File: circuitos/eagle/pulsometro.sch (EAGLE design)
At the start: 35 parts, among them IC1 LM358N, IC2 LM358N, IC3 PIC18F2550_28DIP, T1 BC547, X1 20MHz

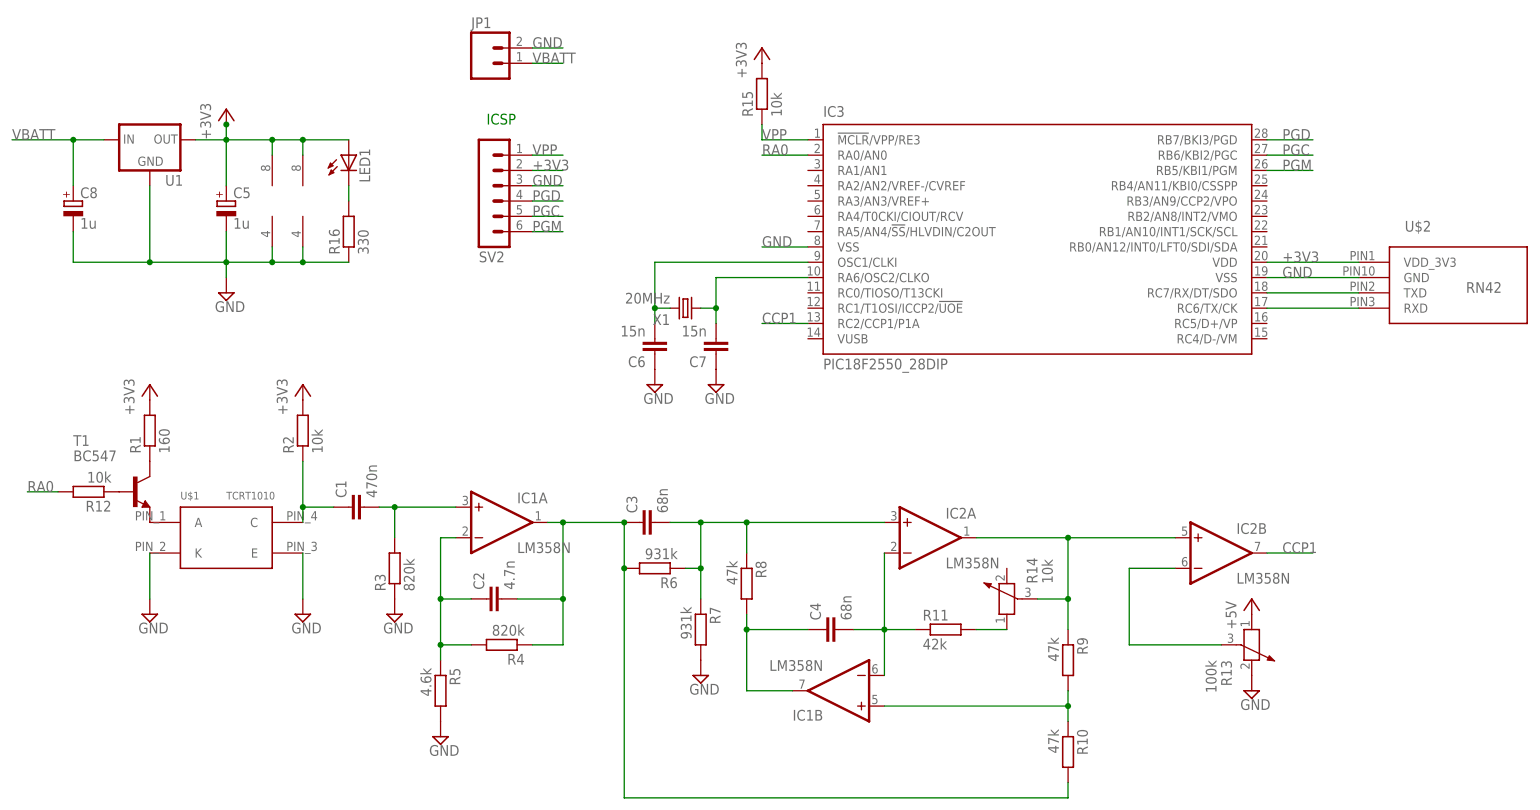
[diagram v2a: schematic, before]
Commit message: Update circuit
* Remove transistor switch of TCRT1010 diode and change resistor value
* Change LM358 op-amp to TLV2472
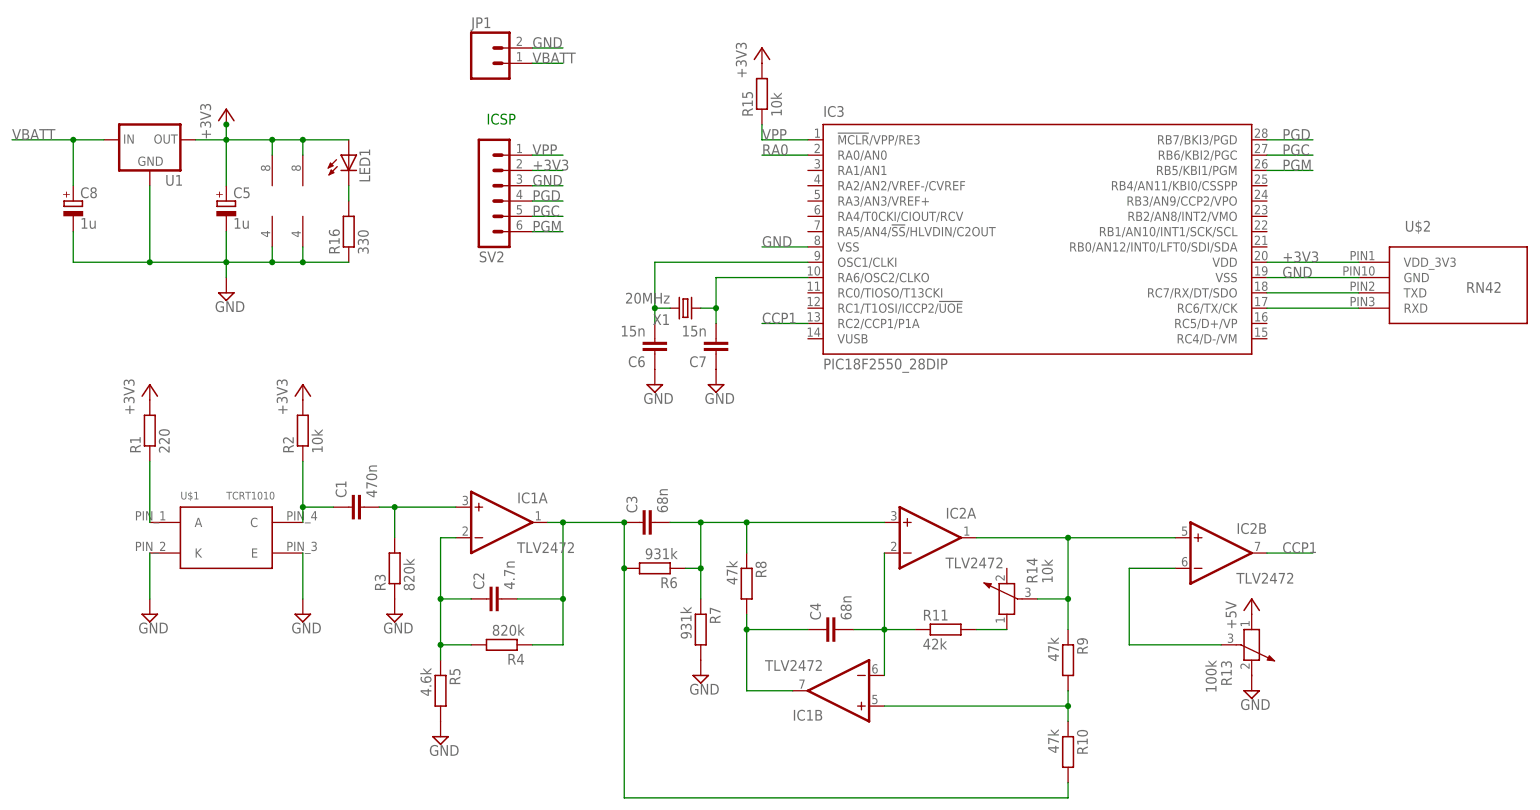
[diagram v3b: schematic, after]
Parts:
- removed R12: 10k, rcl:R-EU_0204/7
- removed T1: BC547, transistor:BC547
- IC1, IC2: value LM358N -> TLV2472
- R1: value 160 -> 220
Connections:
- removed net N$2: T1.E, U$1.A
- removed net N$7: R12.1, T1.B
- net N$1: now also U$1.A; no longer T1.C
- net RA0: no longer R12.2
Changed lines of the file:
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@@
 <grid distance="0.1" unitdist="inch" unit="inch" style="lines" multiple="1" display="no" altdistance="0.01" altunitdist="inch" altunit="inch"/>
 <layers>
-<layer number="1" name="Top" color="4" fill="1" visible="no" active="no"/>
-<layer number="16" name="Bottom" color="1" fill="1" visible="no" active="no"/>
-<layer number="17" name="Pads" color="2" fill="1" visible="no" active="no"/>
-<layer number="18" name="Vias" color="2" fill="1" visible="no" active="no"/>
-<layer number="19" name="Unrouted" color="6" fill="1" visible="no" active="no"/>
-<layer number="20" name="Dimension" color="15" fill="1" visible="no" active="no"/>
-<layer number="21" name="tPlace" color="16" fill="1" visible="no" active="no"/>
-<layer number="22" name="bPlace" color="14" fill="1" visible="no" active="no"/>
-<layer number="23" name="tOrigins" color="15" fill="1" visible="no" active="no"/>
-<layer number="24" name="bOrigins" color="15" fill="1" visible="no" active="no"/>
-<layer number="25" name="tNames" color="7" fill="1" visible="no" active="no"/>
-<layer number="26" name="bNames" color="7" fill="1" visible="no" active="no"/>
-<layer number="27" name="tValues" color="7" fill="1" visible="no" active="no"/>
-<layer number="28" name="bValues" color="7" fill="1" visible="no" active="no"/>
+<layer number="1" name="Top" color="4" fill="1" visible="yes" active="no"/>
+<layer number="16" name="Bottom" color="1" fill="1" visible="yes" active="no"/>
+<layer number="17" name="Pads" color="2" fill="1" visible="yes" active="no"/>
+<layer number="18" name="Vias" color="2" fill="1" visible="yes" active="no"/>
+<layer number="19" name="Unrouted" color="6" fill="1" visible="yes" active="no"/>
+<layer number="20" name="Dimension" color="15" fill="1" visible="yes" active="no"/>
+<layer number="21" name="tPlace" color="16" fill="1" visible="yes" active="no"/>
+<layer number="22" name="bPlace" color="14" fill="1" visible="yes" active="no"/>
+<layer number="23" name="tOrigins" color="15" fill="1" visible="yes" active="no"/>
+<layer number="24" name="bOrigins" color="15" fill="1" visible="yes" active="no"/>
+<layer number="25" name="tNames" color="7" fill="1" visible="yes" active="no"/>
+<layer number="26" name="bNames" color="7" fill="1" visible="yes" active="no"/>
+<layer number="27" name="tValues" color="7" fill="1" visible="yes" active="no"/>
+<layer number="28" name="bValues" color="7" fill="1" visible="yes" active="no"/>
 <layer number="29" name="tStop" color="7" fill="3" visible="no" active="no"/>
 <layer number="30" name="bStop" color="7" fill="6" visible="no" active="no"/>
@@
 <layer number="35" name="tGlue" color="7" fill="4" visible="no" active="no"/>
 <layer number="36" name="bGlue" color="7" fill="5" visible="no" active="no"/>
-<layer number="37" name="tTest" color="7" fill="1" visible="no" active="no"/>
-<layer number="38" name="bTest" color="7" fill="1" visible="no" active="no"/>
+<layer number="37" name="tTest" color="7" fill="1" visible="yes" active="no"/>
+<layer number="38" name="bTest" color="7" fill="1" visible="yes" active="no"/>
 <layer number="39" name="tKeepout" color="4" fill="11" visible="no" active="no"/>
 <layer number="40" name="bKeepout" color="1" fill="11" visible="no" active="no"/>
@@
 <layer number="44" name="Drills" color="7" fill="1" visible="no" active="no"/>
 <layer number="45" name="Holes" color="7" fill="1" visible="no" active="no"/>
-<layer number="46" name="Milling" color="3" fill="1" visible="no" active="no"/>
-<layer number="47" name="Measures" color="7" fill="1" visible="no" active="no"/>
-<layer number="48" name="Document" color="7" fill="1" visible="no" active="no"/>
-<layer number="49" name="Reference" color="7" fill="1" visible="no" active="no"/>
-<layer number="50" name="dxf" color="7" fill="1" visible="no" active="no"/>
-<layer number="51" name="tDocu" color="6" fill="1" visible="no" active="no"/>
-<layer number="52" name="bDocu" color="7" fill="1" visible="no" active="no"/>
-<layer number="53" name="tGND_GNDA" color="7" fill="9" visible="no" active="no"/>
-<layer number="54" name="bGND_GNDA" color="1" fill="9" visible="no" active="no"/>
-<layer number="56" name="wert" color="7" fill="1" visible="no" active="no"/>
-<layer number="57" name="tCAD" color="7" fill="1" visible="no" active="no"/>
-<layer number="59" name="tCarbon" color="7" fill="1" visible="no" active="no"/>
-<layer number="60" name="bCarbon" color="7" fill="1" visible="no" active="no"/>
+<layer number="46" name="Milling" color="3" fill="1" visible="yes" active="no"/>
+<layer number="47" name="Measures" color="7" fill="1" visible="yes" active="no"/>
+<layer number="48" name="Document" color="7" fill="1" visible="yes" active="no"/>
+<layer number="49" name="Reference" color="7" fill="1" visible="yes" active="no"/>
+<layer number="50" name="dxf" color="7" fill="1" visible="yes" active="no"/>
+<layer number="51" name="tDocu" color="6" fill="1" visible="yes" active="no"/>
+<layer number="52" name="bDocu" color="7" fill="1" visible="yes" active="no"/>
+<layer number="53" name="tGND_GNDA" color="7" fill="9" visible="yes" active="no"/>
+<layer number="54" name="bGND_GNDA" color="1" fill="9" visible="yes" active="no"/>
+<layer number="56" name="wert" color="7" fill="1" visible="yes" active="no"/>
+<layer number="57" name="tCAD" color="7" fill="1" visible="yes" active="no"/>
+<layer number="59" name="tCarbon" color="7" fill="1" visible="yes" active="no"/>
+<layer number="60" name="bCarbon" color="7" fill="1" visible="yes" active="no"/>
 <layer number="90" name="Modules" color="5" fill="1" visible="yes" active="yes"/>
 <layer number="91" name="Nets" color="2" fill="1" visible="yes" active="yes"/>
@@
 <part name="SUPPLY4" library="supply2" deviceset="GND" device=""/>
 <part name="P+1" library="supply1" deviceset="+3V3" device=""/>
-<part name="R1" library="rcl" deviceset="R-EU_" device="0204/7" value="160"/>
+<part name="R1" library="rcl" deviceset="R-EU_" device="0204/7" value="220"/>
 <part name="R2" library="rcl" deviceset="R-EU_" device="0204/7" value="10k"/>
-<part name="T1" library="transistor" deviceset="BC547" device=""/>
 <part name="C1" library="rcl" deviceset="C-EU" device="025-025X050" value="470n"/>
 <part name="C2" library="rcl" deviceset="C-EU" device="025-025X050" value="4.7n"/>
@@
 <part name="SUPPLY1" library="supply2" deviceset="GND" device=""/>
 <part name="SUPPLY2" library="supply2" deviceset="GND" device=""/>
-<part name="IC1" library="linear" deviceset="LM358" device="N"/>
+<part name="IC1" library="linear" deviceset="LM358" device="N" value="TLV2472"/>
 <part name="SUPPLY5" library="supply2" deviceset="GND" device=""/>
 <part name="R6" library="rcl" deviceset="R-EU_" device="0204/7" value="931k"/>
@@
 <part name="R10" library="rcl" deviceset="R-EU_" device="0204/7" value="47k"/>
 <part name="R11" library="rcl" deviceset="R-EU_" device="0204/7" value="42k"/>
-<part name="R12" library="rcl" deviceset="R-EU_" device="0204/7" value="10k"/>
 <part name="C3" library="rcl" deviceset="C-EU" device="025-025X050" value="68n"/>
 <part name="C4" library="rcl" deviceset="C-EU" device="025-025X050" value="68n"/>
-<part name="IC2" library="linear" deviceset="LM358" device="N"/>
+<part name="IC2" library="linear" deviceset="LM358" device="N" value="TLV2472"/>
 <part name="R13" library="rcl" deviceset="POTENTIOMETER_" device="PT-10" value="100k"/>
 <part name="R14" library="rcl" deviceset="POTENTIOMETER_" device="PT-10" value="10k"/>
@@
 <instance part="R1" gate="G$1" x="20.32" y="38.1" rot="R90"/>
 <instance part="R2" gate="G$1" x="45.72" y="38.1" rot="R90"/>
-<instance part="T1" gate="G$1" x="17.78" y="27.94"/>
 <instance part="C1" gate="G$1" x="53.34" y="25.4" rot="R90"/>
 <instance part="C2" gate="G$1" x="76.2" y="10.16" rot="R90"/>
@@
 <instance part="R10" gate="G$1" x="172.72" y="-15.24" rot="R270"/>
 <instance part="R11" gate="G$1" x="152.4" y="5.08"/>
-<instance part="R12" gate="G$1" x="10.16" y="27.94" rot="R180"/>
 <instance part="C3" gate="G$1" x="101.6" y="22.86" rot="R90"/>
 <instance part="C4" gate="G$1" x="132.08" y="5.08" rot="R90"/>
@@
 </busses>
 <nets>
-<net name="N$1" class="0">
-<segment>
-<pinref part="R1" gate="G$1" pin="1"/>
-<pinref part="T1" gate="G$1" pin="C"/>
-</segment>
-</net>
-<net name="N$2" class="0">
-<segment>
-<pinref part="U$1" gate="G$1" pin="A"/>
-<pinref part="T1" gate="G$1" pin="E"/>
-</segment>
-</net>
 <net name="+3V3" class="0">
 <segment>
@@
 </segment>
 </net>
-<net name="N$7" class="0">
-<segment>
-<pinref part="T1" gate="G$1" pin="B"/>
-<pinref part="R12" gate="G$1" pin="1"/>
-</segment>
-</net>
 <net name="RA0" class="0">
-<segment>
-<pinref part="R12" gate="G$1" pin="2"/>
-<wire x1="5.08" y1="27.94" x2="0" y2="27.94" width="0.1524" layer="91"/>
-<label x="0" y="27.94" size="1.778" layer="95"/>
-</segment>
 <segment>
 <pinref part="IC3" gate="G$1" pin="RA0/AN0"/>
@@
 </segment>
 </net>
+<net name="N$1" class="0">
+<segment>
+<pinref part="U$1" gate="G$1" pin="A"/>
+<pinref part="R1" gate="G$1" pin="1"/>
+<wire x1="20.32" y1="22.86" x2="20.32" y2="33.02" width="0.1524" layer="91"/>
+</segment>
+</net>

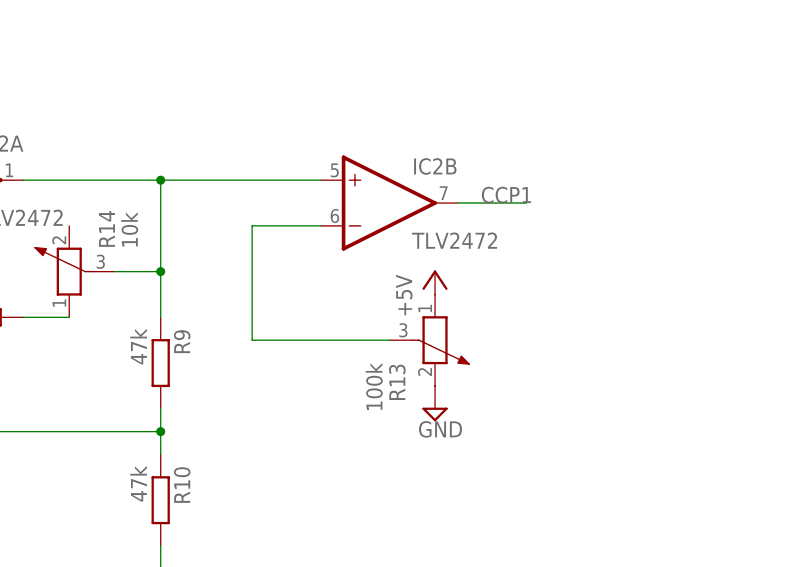
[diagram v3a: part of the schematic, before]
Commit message: Fix voltage source value
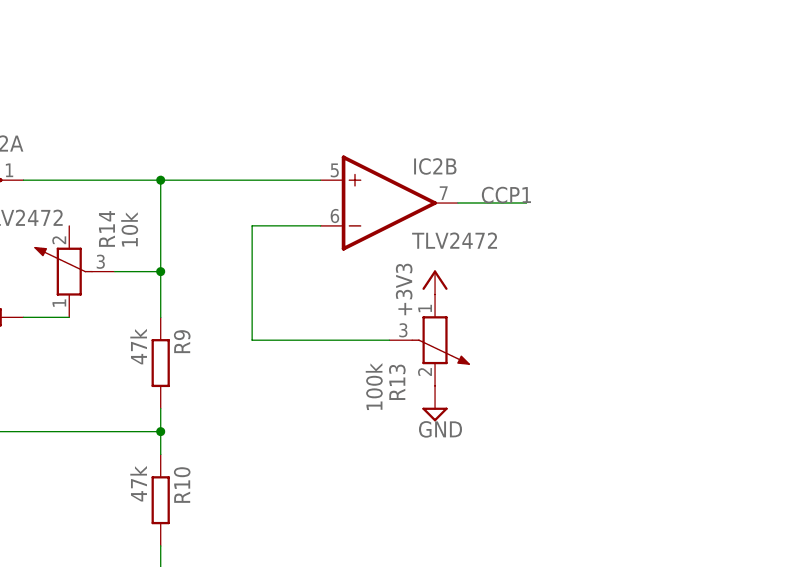
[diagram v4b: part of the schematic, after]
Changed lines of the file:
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@@
 <part name="R14" library="rcl" deviceset="POTENTIOMETER_" device="PT-10" value="10k"/>
 <part name="SUPPLY7" library="supply2" deviceset="GND" device=""/>
-<part name="P+5" library="supply1" deviceset="+5V" device=""/>
 <part name="SUPPLY8" library="supply2" deviceset="GND" device=""/>
 <part name="IC3" library="microchip" deviceset="PIC18F2*_28" device="DIP" technology="550"/>
@@
 <part name="U1" library="SparkFun-PowerIC" deviceset="V_REG_78XX" device="TO-92_UNTESTED"/>
 <part name="C8" library="rcl" deviceset="CPOL-EU" device="E2.5-5" value="1u"/>
+<part name="P+5" library="supply1" deviceset="+3V3" device=""/>
 </parts>
 <sheets>
@@
 <instance part="IC2" gate="P" x="45.72" y="76.2"/>
 <instance part="SUPPLY7" gate="GND" x="111.76" y="-2.54"/>
-<instance part="P+5" gate="1" x="203.2" y="10.16"/>
 <instance part="SUPPLY8" gate="GND" x="203.2" y="-5.08"/>
 <instance part="IC3" gate="G$1" x="167.64" y="71.12"/>
@@
 <instance part="U1" gate="G$1" x="20.32" y="86.36"/>
 <instance part="C8" gate="G$1" x="7.62" y="76.2"/>
+<instance part="P+5" gate="G$1" x="203.2" y="10.16"/>
 </instances>
 <busses>
@@
 <pinref part="R1" gate="G$1" pin="2"/>
 <pinref part="P+1" gate="G$1" pin="+3V3"/>
-</segment>
-<segment>
-<pinref part="R13" gate="1" pin="1"/>
-<pinref part="P+5" gate="1" pin="+5V"/>
 </segment>
 <segment>
@@
 <pinref part="P+4" gate="G$1" pin="+3V3"/>
 </segment>
+<segment>
+<pinref part="R13" gate="1" pin="1"/>
+<pinref part="P+5" gate="G$1" pin="+3V3"/>
+</segment>
 </net>

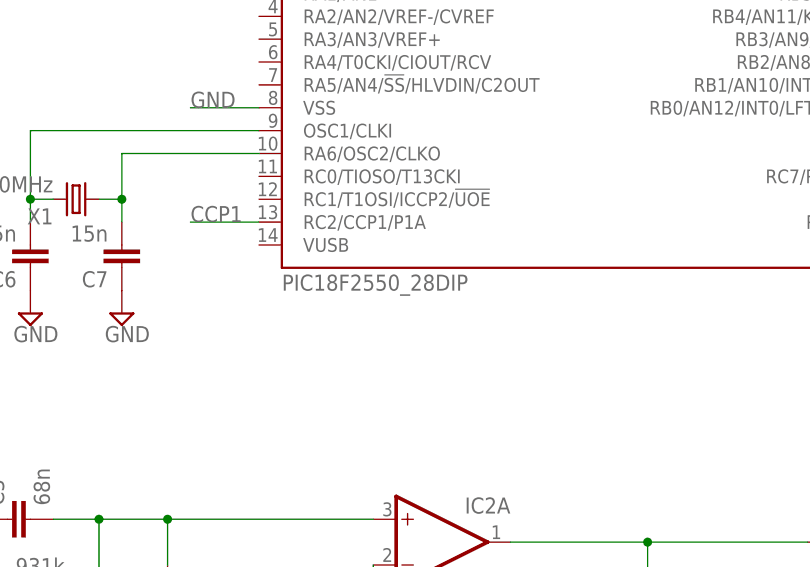
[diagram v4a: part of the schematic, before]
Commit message: Include pcb in report
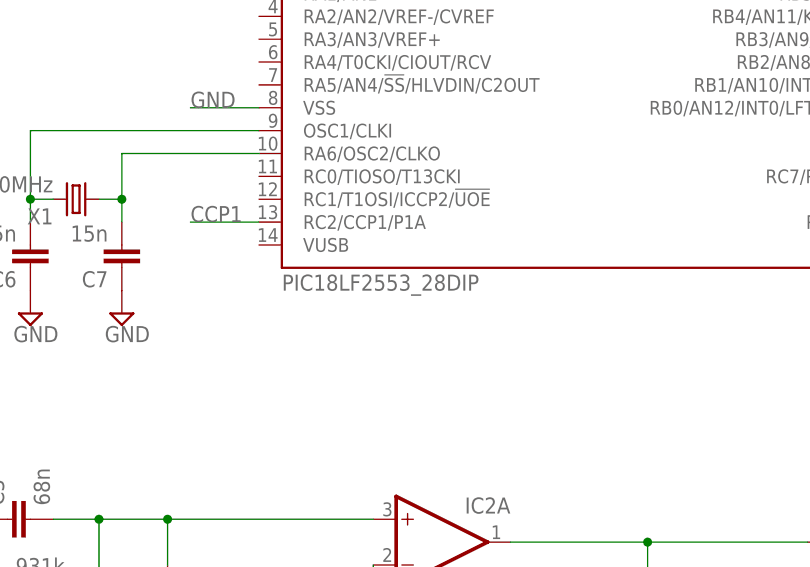
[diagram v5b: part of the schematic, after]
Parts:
- IC3: value PIC18F2550_28DIP -> PIC18LF2553_28DIP
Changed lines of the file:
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@@
 <part name="SUPPLY7" library="supply2" deviceset="GND" device=""/>
 <part name="SUPPLY8" library="supply2" deviceset="GND" device=""/>
-<part name="IC3" library="microchip" deviceset="PIC18F2*_28" device="DIP" technology="550"/>
+<part name="IC3" library="microchip" deviceset="PIC18F2*_28" device="DIP" technology="550" value="PIC18LF2553_28DIP"/>
 <part name="R15" library="rcl" deviceset="R-EU_" device="0204/7" value="10k"/>
 <part name="C5" library="rcl" deviceset="CPOL-EU" device="E2.5-5" value="1u"/>
